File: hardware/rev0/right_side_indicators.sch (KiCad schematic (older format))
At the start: 1 part, among them IC1 ECP5-BGA256

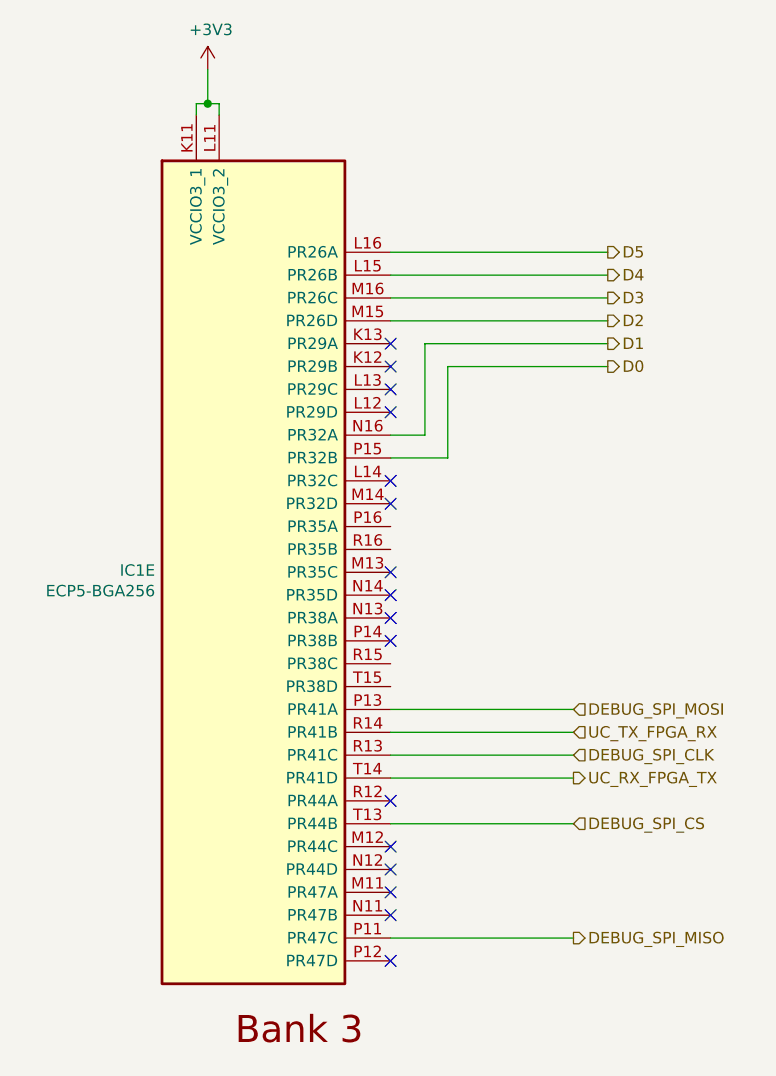
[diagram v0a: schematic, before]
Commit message: Route/NC remaining target signals, ERC & schematic cleanup
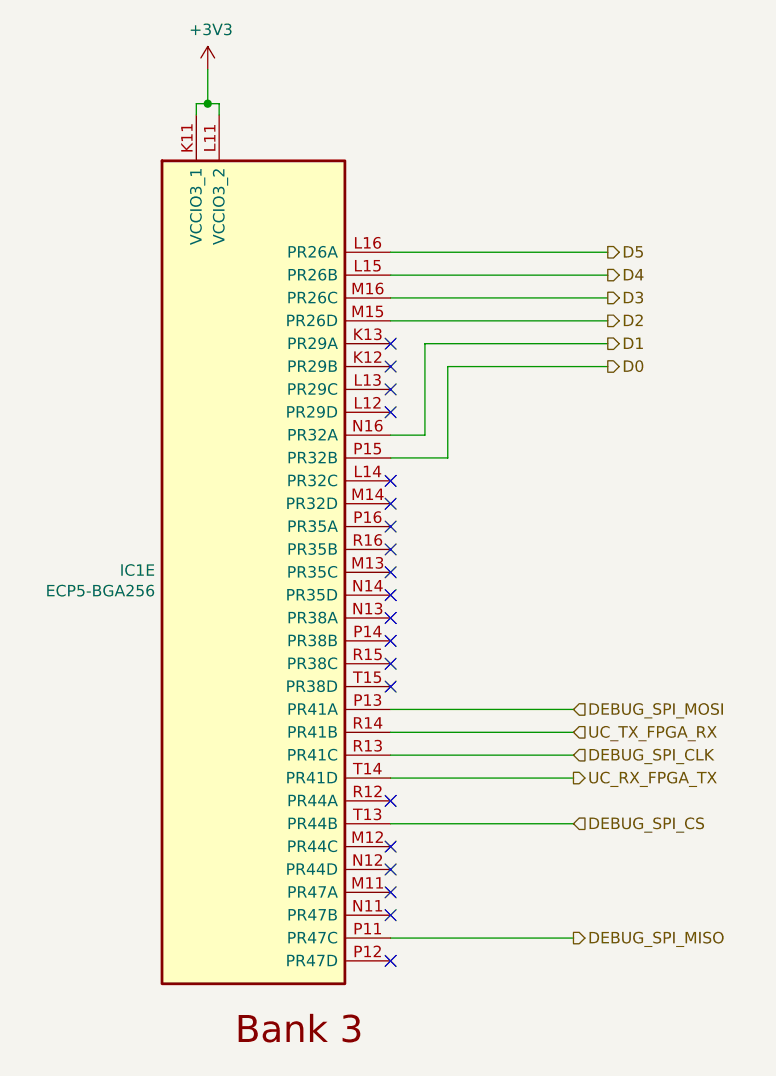
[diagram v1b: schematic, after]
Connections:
- no-connect marks 16 -> 20
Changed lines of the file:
@@
 Wire Wire Line
 	3150 4600 3950 4600
+NoConn ~ 3150 3600
+NoConn ~ 3150 3700
+NoConn ~ 3150 4200
+NoConn ~ 3150 4300
 $EndSCHEMATC

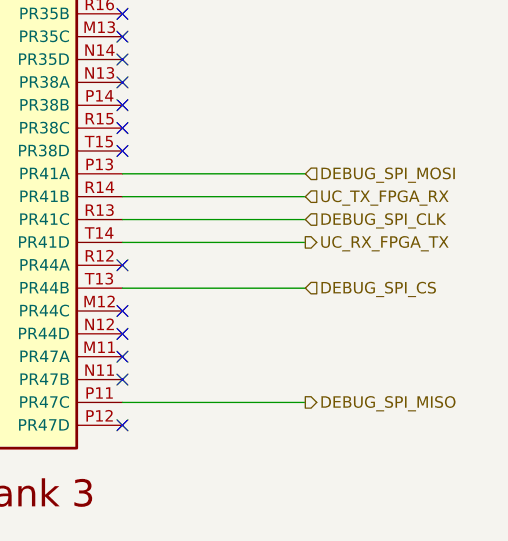
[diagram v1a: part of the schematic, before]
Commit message: hardware: adopt OSHWA convention for SPI signal names
https://www.oshwa.org/a-resolution-to-redefine-spi-signal-names
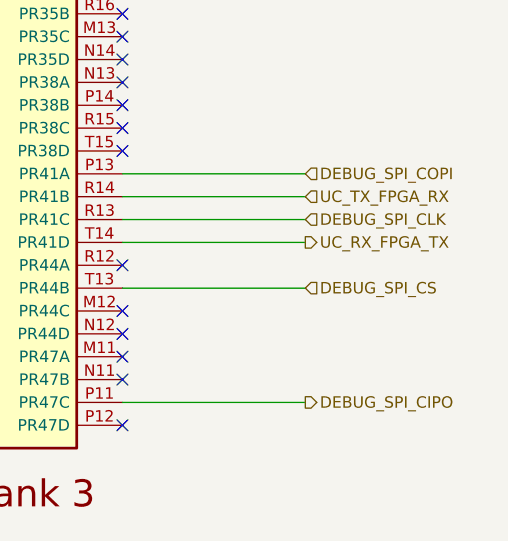
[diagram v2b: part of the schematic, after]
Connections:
- net DEBUG_SPI_MISO renamed DEBUG_SPI_CIPO
- net DEBUG_SPI_MOSI renamed DEBUG_SPI_COPI
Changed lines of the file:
@@
 	3150 4400 3950 4400
 Text HLabel 3950 5400 2    50   Output ~ 0
-DEBUG_SPI_MISO
+DEBUG_SPI_CIPO
 Text HLabel 3950 4600 2    50   Input ~ 0
 DEBUG_SPI_CLK
 Text HLabel 3950 4400 2    50   Input ~ 0
-DEBUG_SPI_MOSI
+DEBUG_SPI_COPI
 Text HLabel 3950 4900 2    50   Input ~ 0
 DEBUG_SPI_CS
